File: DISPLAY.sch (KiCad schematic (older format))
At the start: 2 parts

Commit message: added additional IO expanders
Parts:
- removed U?: 74HC595, symbol 74xx:74HC595
- added C15, C17: 0.1uF, symbol Device:C
- added U10, U9: MCP23008-xP, Package_DIP:DIP-18_W7.62mm, symbol Interface_Expansion:MCP23008-xP
- gave numbers to parts that had none: 1
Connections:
- net labels added: MOSI_SDA, RST, SCK_SCL
- wire segments 22 -> 70
- no-connect marks 1 -> 7
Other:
- moved on the sheet: DS1

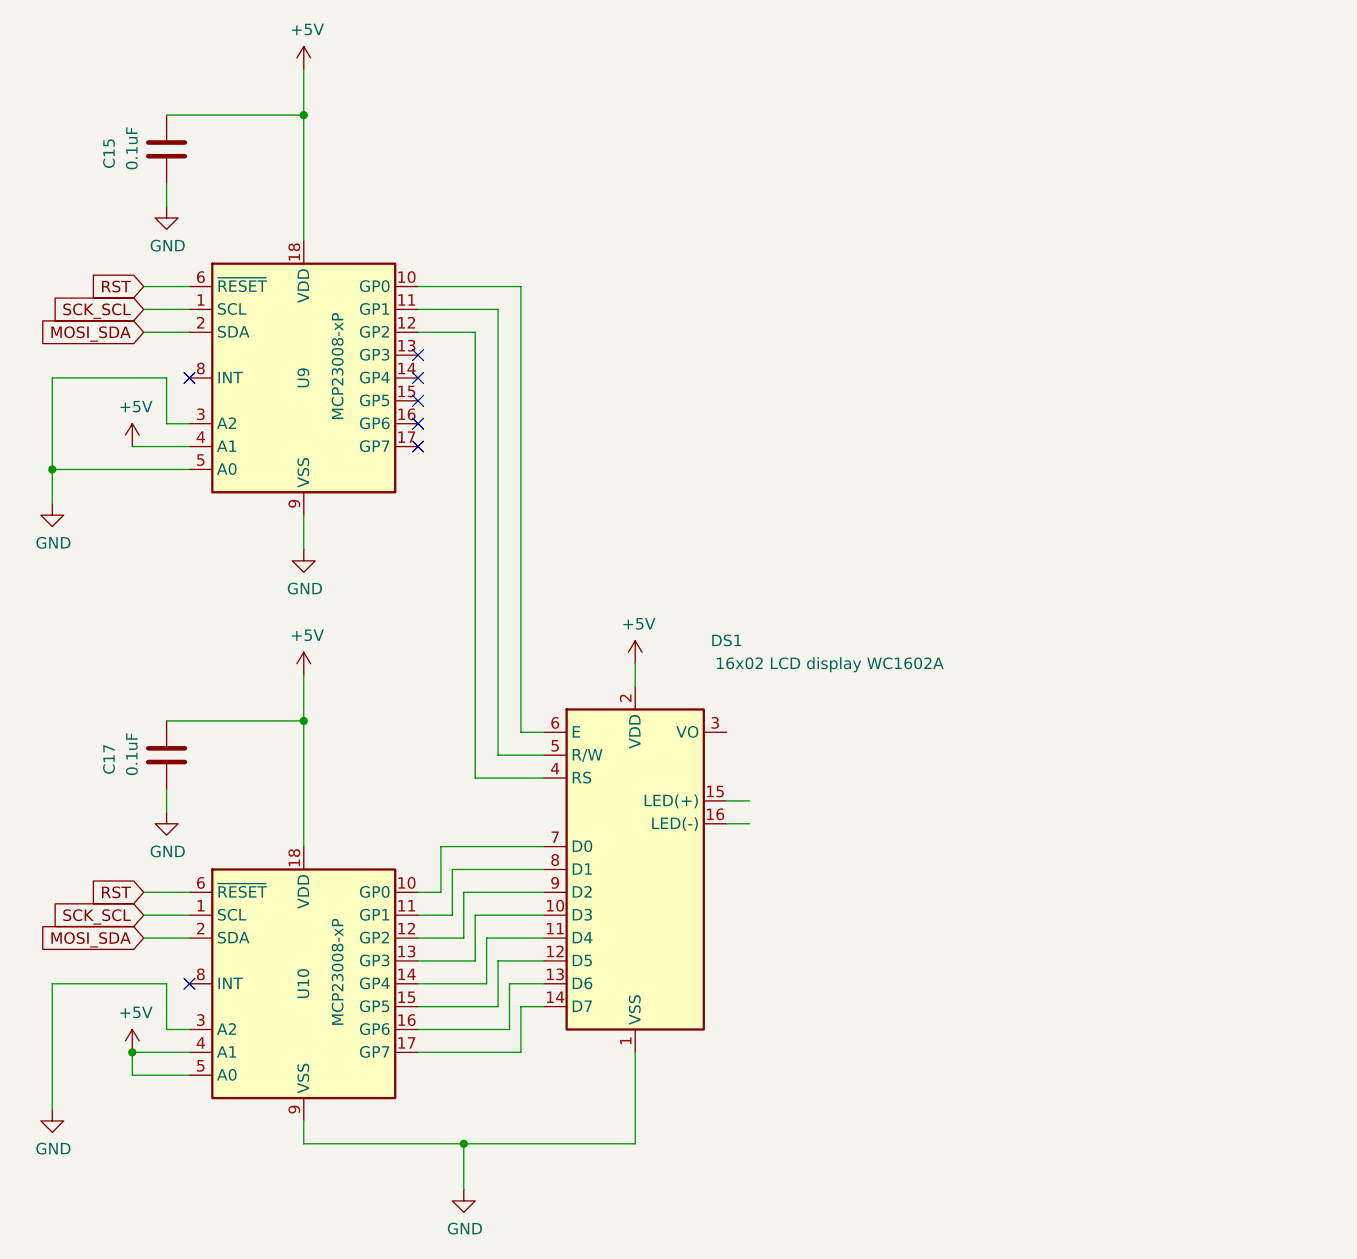
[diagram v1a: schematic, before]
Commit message: Switched the MCU to a basic STM32, changed the business logic to 3V3, created a new 3V3 regulator for this. Also initialised code base. We'll use ARM Mbed for rapid development
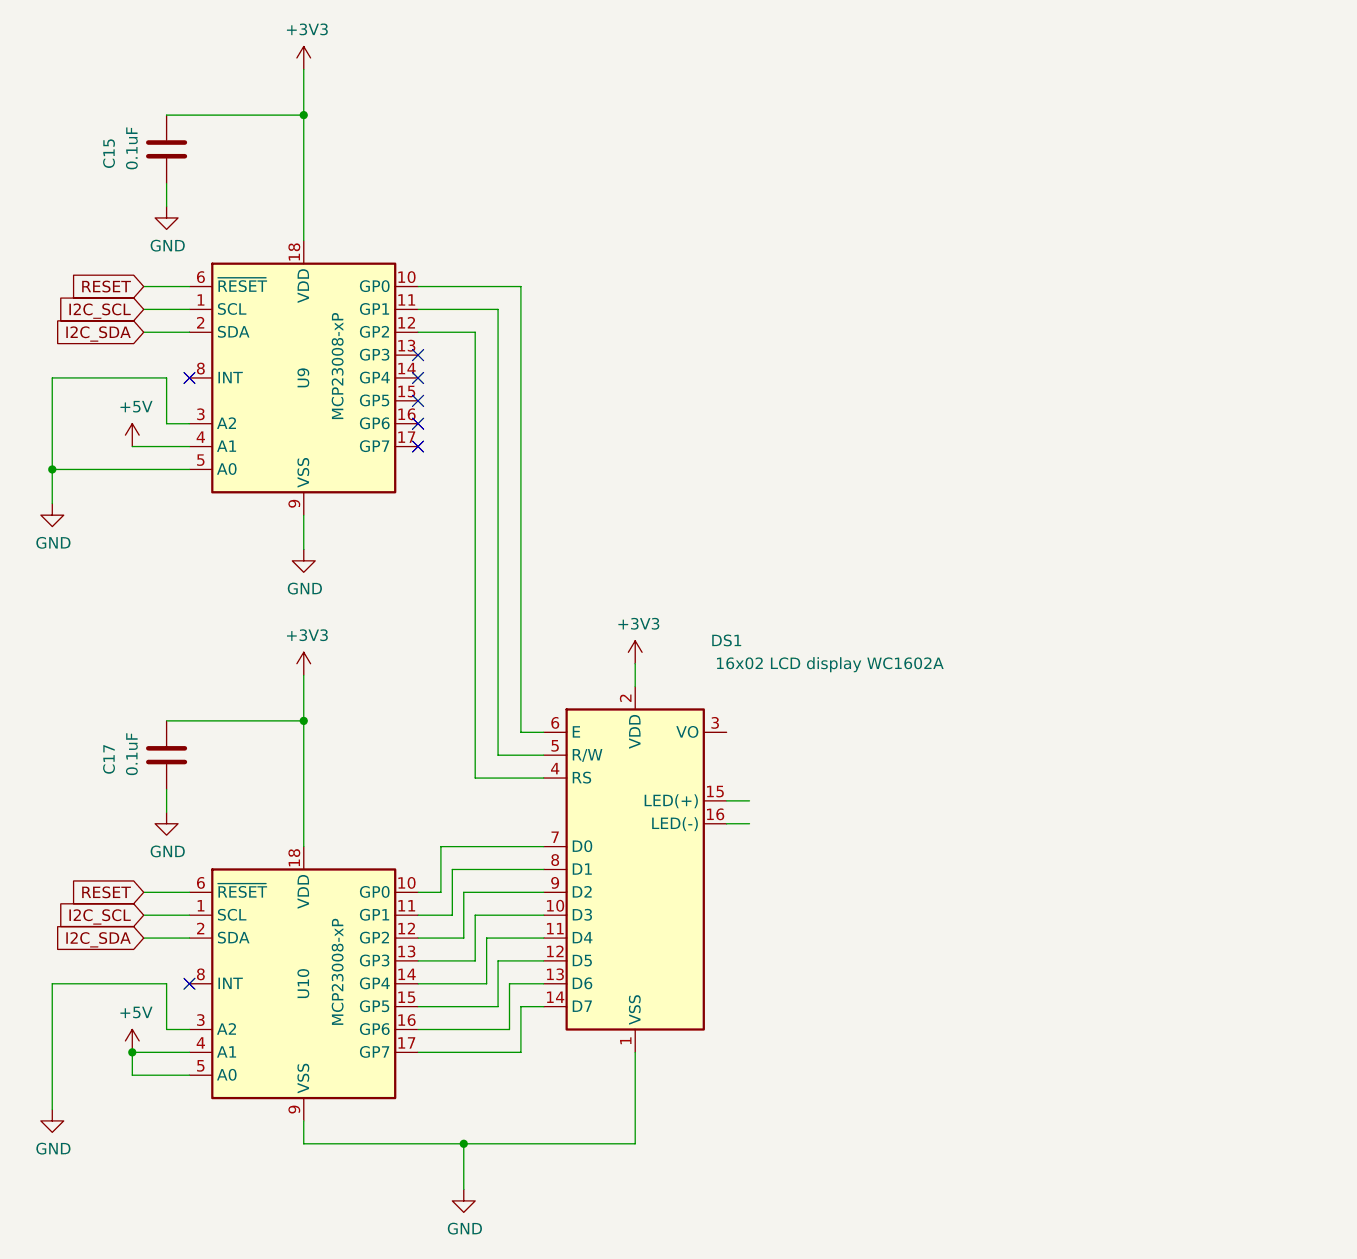
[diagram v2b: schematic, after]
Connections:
- net +5V: no longer C15.2, C17.2, DS1.2 (VDD), U10.18 (VDD), U9.18 (VDD)
- net MOSI_SDA renamed I2C_SDA
- net RST renamed RESET
- net SCK_SCL renamed I2C_SCL
- new net +3V3: C15.2, C17.2, DS1.2 (VDD), U10.18 (VDD), U9.18 (VDD)
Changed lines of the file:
@@
-	1    0    0    -1
-$EndComp
-$Comp
-L power:+5V #PWR021
-U 1 1 60976139
-P 4900 4400
-F 0 "#PWR021" H 4900 4250 50  0001 C CNN
-F 1 "+5V" H 4915 4573 50  0000 C CNN
-F 2 "" H 4900 4400 50  0001 C CNN
-F 3 "" H 4900 4400 50  0001 C CNN
-	1    4900 4400
 	1    0    0    -1
 $EndComp
@@
 	1    0    0    -1
 $EndComp
-Text GLabel 2750 5400 0    50   Input ~ 0
-RST
 Wire Wire Line
 	2950 5400 2750 5400
-Text GLabel 2750 5500 0    50   Input ~ 0
-SCK_SCL
-Text GLabel 2750 5600 0    50   Input ~ 0
-MOSI_SDA
 Wire Wire Line
 	2950 5500 2750 5500
@@
 	3450 4650 3450 4450
 Connection ~ 3450 4650
-$Comp
-L power:+5V #PWR?
-U 1 1 5FEF98F4
-P 3450 4450
-AR Path="/5FEF98F4" Ref="#PWR?"  Part="1"
-AR Path="/604E5285/5FEF98F4" Ref="#PWR?"  Part="1"
-AR Path="/6096B205/5FEF98F4" Ref="#PWR019"  Part="1"
-F 0 "#PWR019" H 3450 4300 50  0001 C CNN
-F 1 "+5V" H 3465 4623 50  0000 C CNN
-F 2 "" H 3450 4450 50  0001 C CNN
-F 3 "" H 3450 4450 50  0001 C CNN
-	1    3450 4450
-	1    0    0    -1
-$EndComp
-Text GLabel 2750 2750 0    50   Input ~ 0
-RST
 Wire Wire Line
 	2950 2750 2750 2750
-Text GLabel 2750 2850 0    50   Input ~ 0
-SCK_SCL
-Text GLabel 2750 2950 0    50   Input ~ 0
-MOSI_SDA
 Wire Wire Line
 	2950 2850 2750 2850
@@
 	3450 2000 3450 1800
 Connection ~ 3450 2000
-$Comp
-L power:+5V #PWR?
-U 1 1 5FEFB8FA
-P 3450 1800
-AR Path="/5FEFB8FA" Ref="#PWR?"  Part="1"
-AR Path="/604E5285/5FEFB8FA" Ref="#PWR?"  Part="1"
-AR Path="/6096B205/5FEFB8FA" Ref="#PWR017"  Part="1"
-F 0 "#PWR017" H 3450 1650 50  0001 C CNN
-F 1 "+5V" H 3465 1973 50  0000 C CNN
-F 2 "" H 3450 1800 50  0001 C CNN
-F 3 "" H 3450 1800 50  0001 C CNN
-	1    3450 1800
-	1    0    0    -1
-$EndComp
 NoConn ~ 3950 3350
 NoConn ~ 3950 3450
@@
 	4900 6500 4150 6500
 Connection ~ 4150 6500
+Text GLabel 2750 5500 0    50   Input ~ 0
+I2C_SCL
+Text GLabel 2750 5600 0    50   Input ~ 0
+I2C_SDA
+Text GLabel 2750 2850 0    50   Input ~ 0
+I2C_SCL
+Text GLabel 2750 2950 0    50   Input ~ 0
+I2C_SDA
+Text GLabel 2750 5400 0    50   Input ~ 0
+RESET
+Text GLabel 2750 2750 0    50   Input ~ 0
+RESET
+$Comp
+L power:+3V3 #PWR?
+U 1 1 600CDA04
+P 3450 1800
+AR Path="/604E5285/600CDA04" Ref="#PWR?"  Part="1"
+AR Path="/6096B205/600CDA04" Ref="#PWR?"  Part="1"
+F 0 "#PWR?" H 3450 1650 50  0001 C CNN
+F 1 "+3V3" H 3465 1973 50  0000 C CNN
+F 2 "" H 3450 1800 50  0001 C CNN
+F 3 "" H 3450 1800 50  0001 C CNN
+	1    3450 1800
+	1    0    0    -1
+$EndComp
+$Comp
+L power:+3V3 #PWR?
+U 1 1 600D0A68
+P 3450 4450
+AR Path="/604E5285/600D0A68" Ref="#PWR?"  Part="1"
+AR Path="/6096B205/600D0A68" Ref="#PWR?"  Part="1"
+F 0 "#PWR?" H 3450 4300 50  0001 C CNN
+F 1 "+3V3" H 3465 4623 50  0000 C CNN
+F 2 "" H 3450 4450 50  0001 C CNN
+F 3 "" H 3450 4450 50  0001 C CNN
+	1    3450 4450
+	1    0    0    -1
+$EndComp
+$Comp
+L power:+3V3 #PWR?
+U 1 1 600D354A
+P 4900 4400
+AR Path="/604E5285/600D354A" Ref="#PWR?"  Part="1"
+AR Path="/6096B205/600D354A" Ref="#PWR?"  Part="1"
+F 0 "#PWR?" H 4900 4250 50  0001 C CNN
+F 1 "+3V3" H 4915 4573 50  0000 C CNN
+F 2 "" H 4900 4400 50  0001 C CNN
+F 3 "" H 4900 4400 50  0001 C CNN
+	1    4900 4400
+	1    0    0    -1
+$EndComp
 $EndSCHEMATC

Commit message: had to reload source files. Waiting on the STM32F01 so will compile for target STM32F303 for now. Just a temporary change for now
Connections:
- net GND: now also DS1.16 (LED(-))
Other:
- note added: "TODO!!!"
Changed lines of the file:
@@
 Wire Wire Line
 	4150 6500 4150 6700
-Wire Wire Line
-	5300 5000 5400 5000
-Wire Wire Line
-	5300 5100 5400 5100
 $Comp
 L power:GND #PWR020
@@
 	1    0    0    -1
 $EndComp
+Wire Wire Line
+	5700 5100 5700 6500
+Wire Wire Line
+	5700 6500 4900 6500
+Wire Wire Line
+	5300 5100 5700 5100
+Connection ~ 4900 6500
+Wire Wire Line
+	5300 5000 5700 5000
+Wire Wire Line
+	5300 4700 5700 4700
+Text Notes 5750 4850 0    50   ~ 0
+TODO!!!
 $EndSCHEMATC

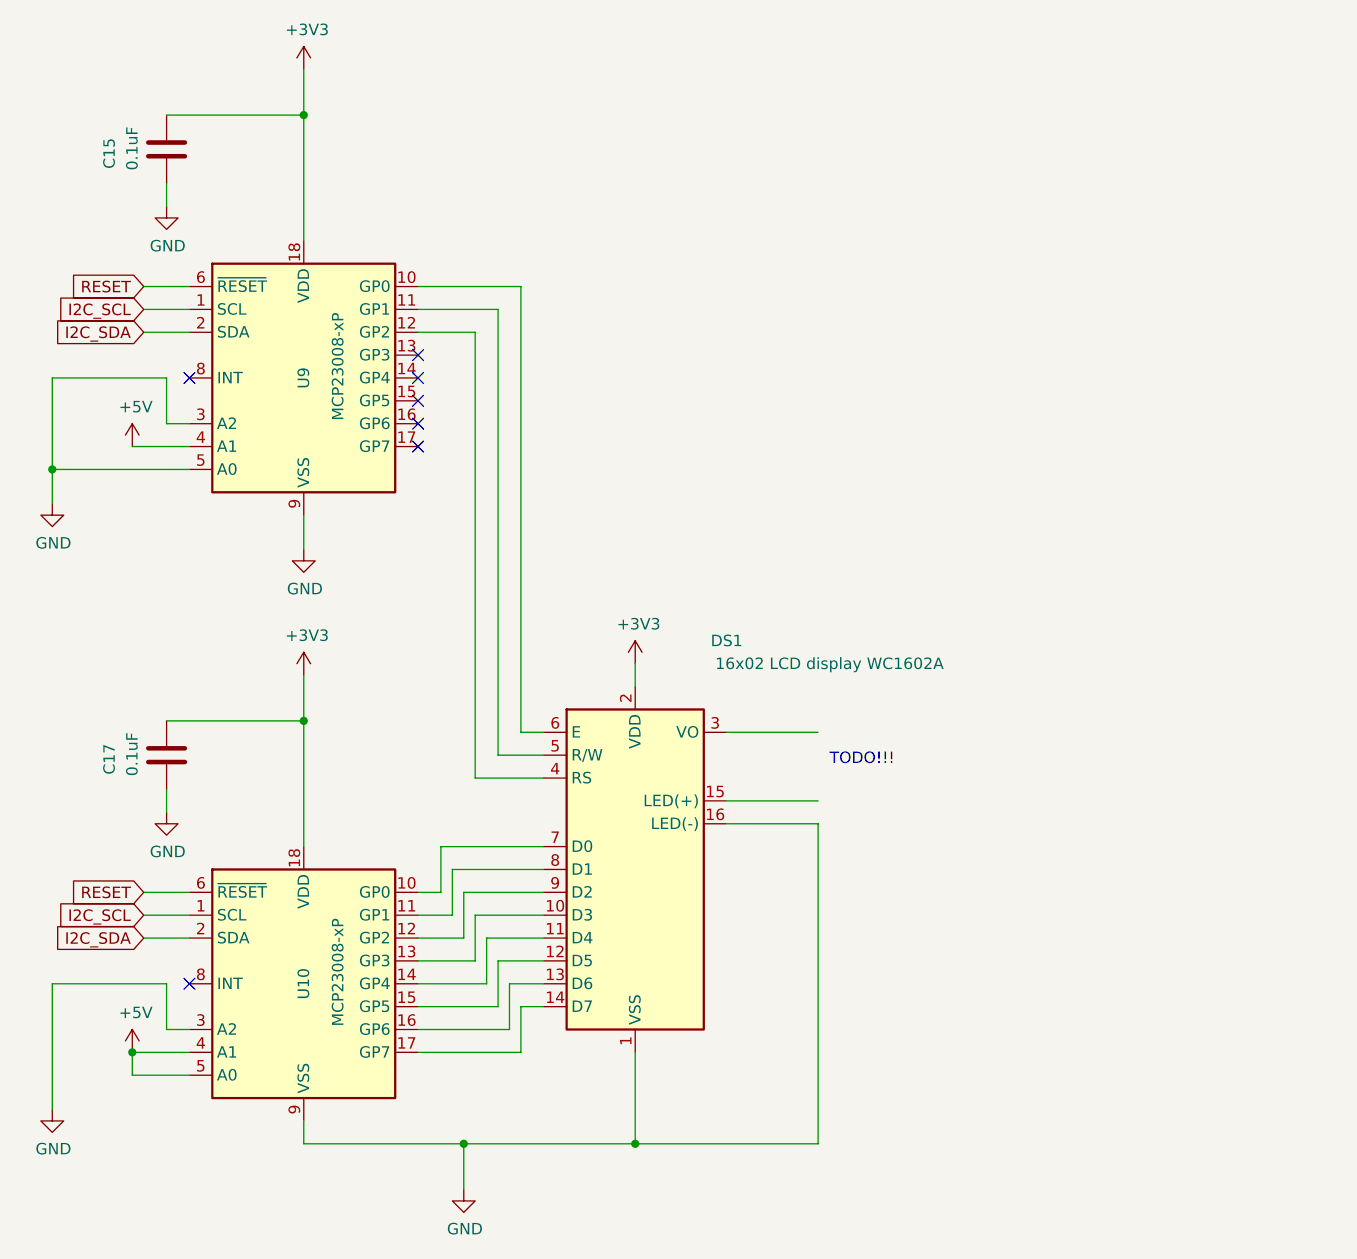
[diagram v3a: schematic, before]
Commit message: We now have more MCU pins. Was able to remove two I2C IO expanders
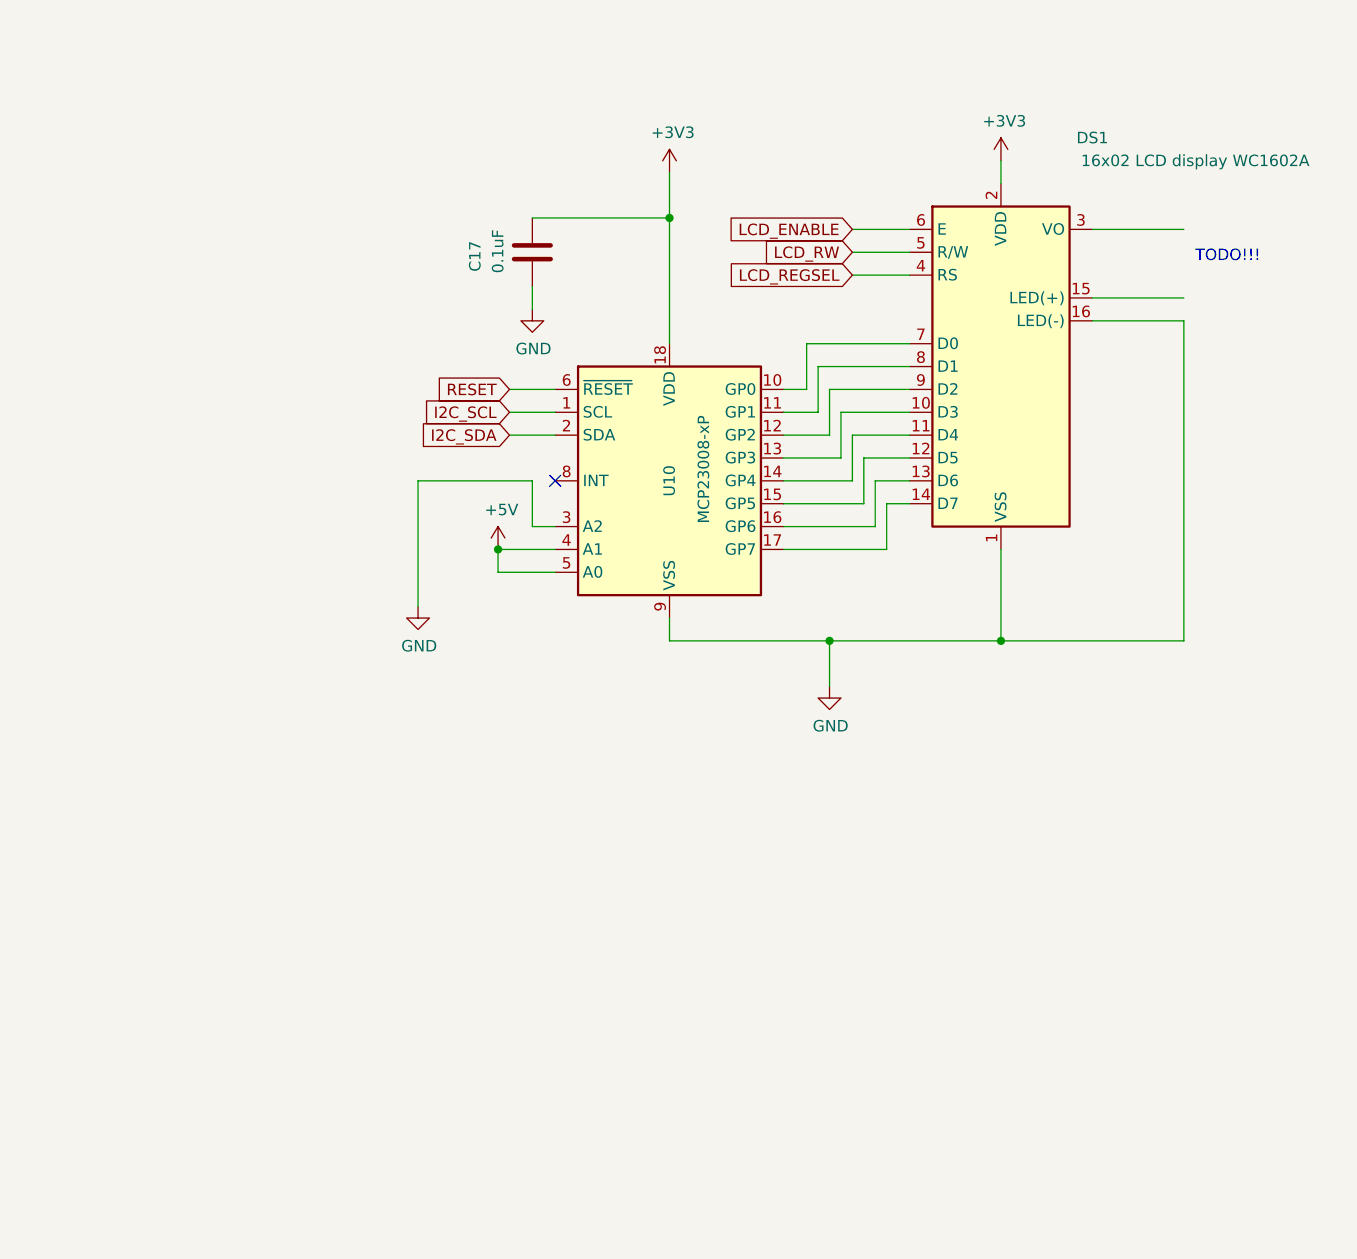
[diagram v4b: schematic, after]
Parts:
- removed C15: 0.1uF, symbol Device:C
- removed U9: MCP23008-xP, Package_DIP:DIP-18_W7.62mm, symbol Interface_Expansion:MCP23008-xP
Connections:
- net labels added: LCD_ENABLE, LCD_REGSEL, LCD_RW
- wire segments 73 -> 52
- no-connect marks 7 -> 1
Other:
- moved on the sheet: C17, DS1, U10

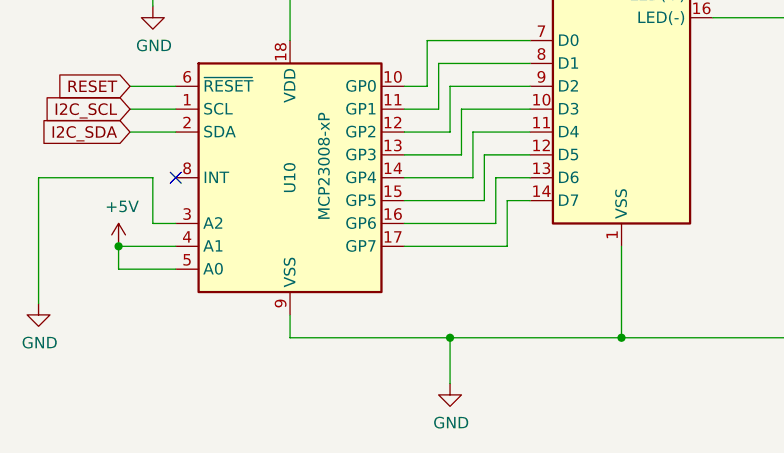
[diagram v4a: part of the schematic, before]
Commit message: fixed some DRC errors
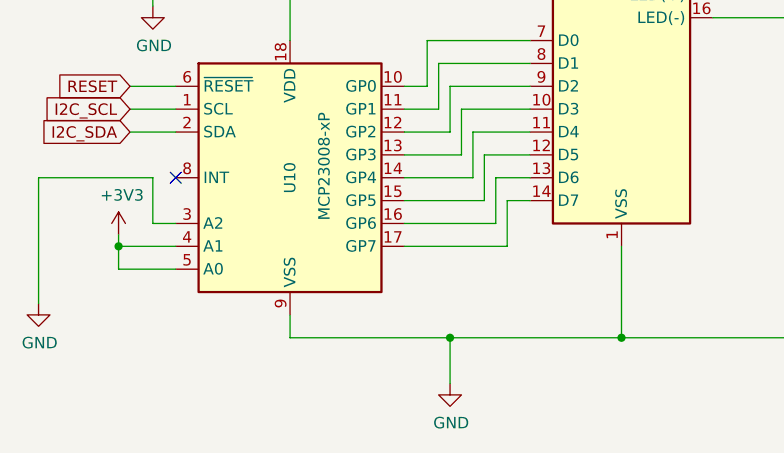
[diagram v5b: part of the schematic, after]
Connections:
- net labels removed: +5V
- wire segments 52 -> 53
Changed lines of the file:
@@
 Wire Wire Line
 	6500 3900 6500 4300
-Wire Wire Line
-	5750 4300 5750 4500
 $Comp
 L power:GND #PWR020
@@
 Connection ~ 5050 2450
 Wire Wire Line
-	5750 4300 5050 4300
-Wire Wire Line
 	5050 4300 5050 4200
 Wire Wire Line
@@
 Wire Wire Line
 	6000 3700 6100 3700
-$Comp
-L power:+5V #PWR?
-U 1 1 5FF50771
-P 4300 3900
-AR Path="/5FF50771" Ref="#PWR?"  Part="1"
-AR Path="/604E5285/5FF50771" Ref="#PWR?"  Part="1"
-AR Path="/6096B205/5FF50771" Ref="#PWR014"  Part="1"
-F 0 "#PWR014" H 4300 3750 50  0001 C CNN
-F 1 "+5V" H 4315 4073 50  0000 C CNN
-F 2 "" H 4300 3900 50  0001 C CNN
-F 3 "" H 4300 3900 50  0001 C CNN
-	1    4300 3900
-	1    0    0    -1
-$EndComp
 $Comp
 L power:GND #PWR?
@@
 Wire Wire Line
 	4300 4000 4300 3900
-Connection ~ 4300 3900
-Wire Wire Line
-	6500 4300 5750 4300
-Connection ~ 5750 4300
 Text GLabel 4350 3300 0    50   Input ~ 0
 I2C_SCL
@@
 P 5050 2250
 AR Path="/604E5285/600D0A68" Ref="#PWR?"  Part="1"
-AR Path="/6096B205/600D0A68" Ref="#PWR?"  Part="1"
-F 0 "#PWR?" H 5050 2100 50  0001 C CNN
+AR Path="/6096B205/600D0A68" Ref="#PWR0112"  Part="1"
+F 0 "#PWR0112" H 5050 2100 50  0001 C CNN
 F 1 "+3V3" H 5065 2423 50  0000 C CNN
 F 2 "" H 5050 2250 50  0001 C CNN
@@
 P 6500 2200
 AR Path="/604E5285/600D354A" Ref="#PWR?"  Part="1"
-AR Path="/6096B205/600D354A" Ref="#PWR?"  Part="1"
-F 0 "#PWR?" H 6500 2050 50  0001 C CNN
+AR Path="/6096B205/600D354A" Ref="#PWR0113"  Part="1"
+F 0 "#PWR0113" H 6500 2050 50  0001 C CNN
 F 1 "+3V3" H 6515 2373 50  0000 C CNN
 F 2 "" H 6500 2200 50  0001 C CNN
@@
 Wire Wire Line
 	6900 2800 7300 2800
-Wire Wire Line
-	6900 2500 7300 2500
 Text Notes 7350 2650 0    50   ~ 0
 TODO!!!
@@
 Text GLabel 5850 2700 0    50   Input ~ 0
 LCD_REGSEL
+Wire Wire Line
+	6900 2500 7300 2500
+Wire Wire Line
+	5050 4300 5750 4300
+Wire Wire Line
+	5750 4500 5750 4300
+Connection ~ 5750 4300
+Wire Wire Line
+	5750 4300 6500 4300
+$Comp
+L power:+3V3 #PWR?
+U 1 1 5FF66CA5
+P 4300 3850
+AR Path="/604E5285/5FF66CA5" Ref="#PWR?"  Part="1"
+AR Path="/6096B205/5FF66CA5" Ref="#PWR0115"  Part="1"
+F 0 "#PWR0115" H 4300 3700 50  0001 C CNN
+F 1 "+3V3" H 4315 4023 50  0000 C CNN
+F 2 "" H 4300 3850 50  0001 C CNN
+F 3 "" H 4300 3850 50  0001 C CNN
+	1    4300 3850
+	1    0    0    -1
+$EndComp
+Wire Wire Line
+	4300 3850 4300 3900
+Connection ~ 4300 3900
 $EndSCHEMATC
